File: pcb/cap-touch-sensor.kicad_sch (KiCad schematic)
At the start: 12 parts, among them U4 CAP1296-x-AIA

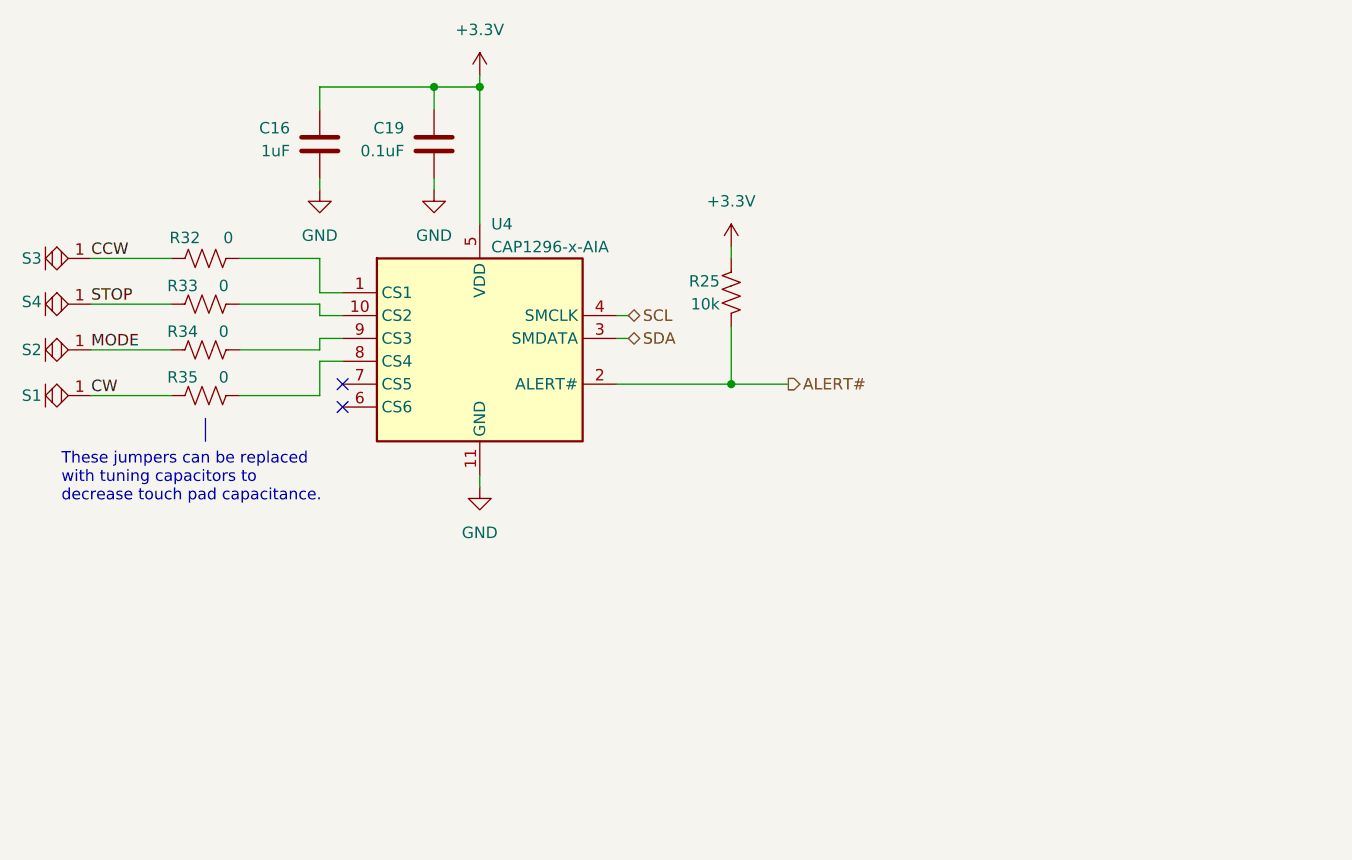
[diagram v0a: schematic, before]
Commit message: Final edits to rev G before fab
- Move USB connector twoards board edge by 1.5mm
- Make all silk text uniform
- Add required stackup and board characteristics to user.comments layer
- Redo 3.3V power routing to RP2040 (one power pin was not connected)
- Uniform schematic sheet size
- And many other small changes
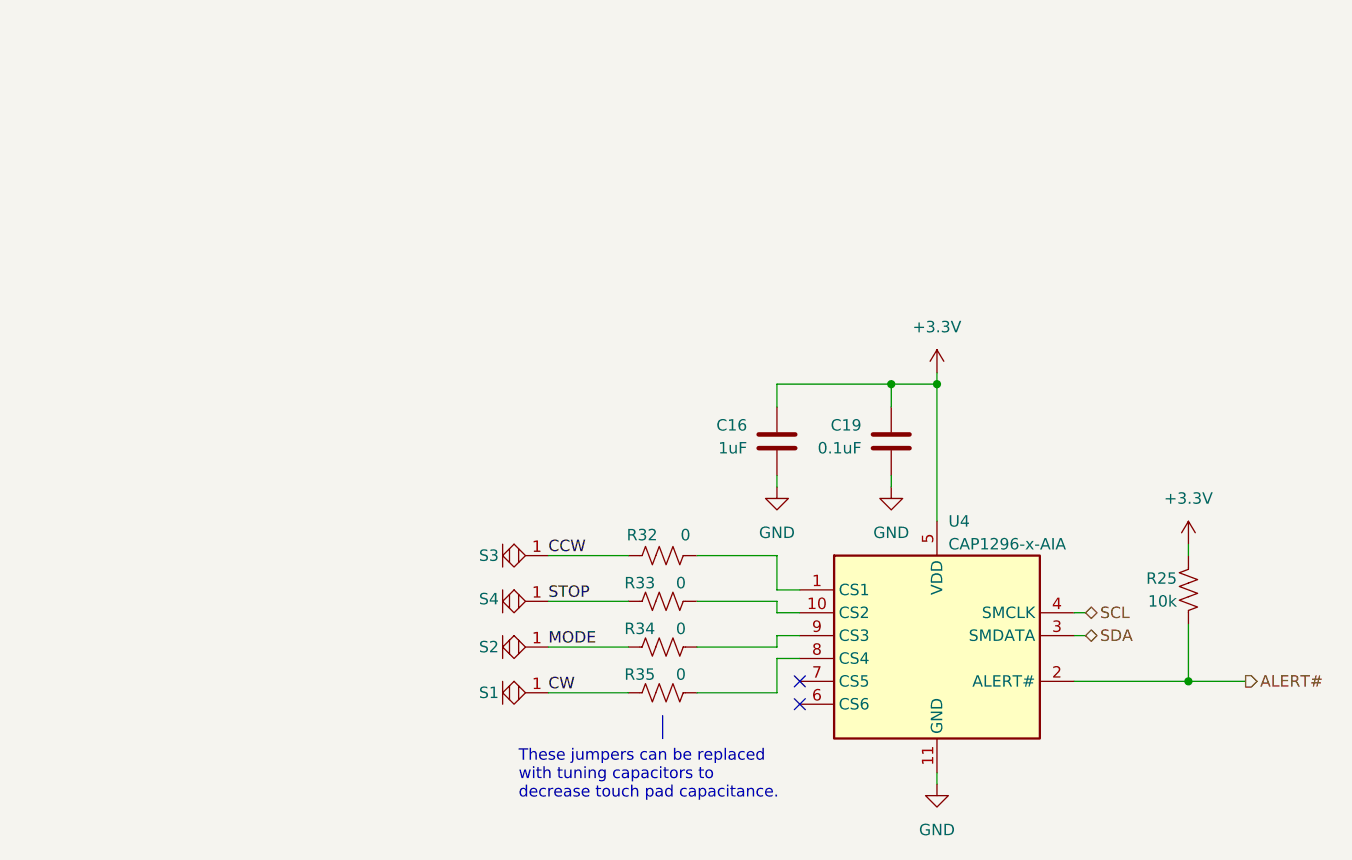
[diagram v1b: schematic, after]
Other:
- moved on the sheet: C16, C19, R25, R32, R33, R34, R35, S1, S2, S3, S4, U4
